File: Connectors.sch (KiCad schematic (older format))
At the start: 0 parts

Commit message: Added symbols to new sheet.
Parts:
- added J?: Conn_01x09, symbol Connector_Generic:Conn_01x09
- added J? (x2): Conn_01x04, symbol Connector_Generic:Conn_01x04
- added J?: Conn_02x03_Odd_Even, symbol Connector_Generic:Conn_02x03_Odd_Even
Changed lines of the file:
@@
 Comment4 "Aurthor: Brycen Dhom"
 $EndDescr
+$Comp
+L Connector_Generic:Conn_01x09 J?
+U 1 1 60175092
+P 3625 3575
+F 0 "J?" H 3705 3617 50  0000 L CNN
+F 1 "Conn_01x09" H 3705 3526 50  0000 L CNN
+F 2 "" H 3625 3575 50  0001 C CNN
+F 3 "~" H 3625 3575 50  0001 C CNN
+	1    3625 3575
+	1    0    0    -1
+$EndComp
+$Comp
+L Connector_Generic:Conn_01x04 J?
+U 1 1 60176115
+P 4775 3300
+F 0 "J?" H 4855 3292 50  0000 L CNN
+F 1 "Conn_01x04" H 4855 3201 50  0000 L CNN
+F 2 "" H 4775 3300 50  0001 C CNN
+F 3 "~" H 4775 3300 50  0001 C CNN
+	1    4775 3300
+	1    0    0    -1
+$EndComp
+$Comp
+L Connector_Generic:Conn_02x03_Odd_Even J?
+U 1 1 6017679C
+P 3575 4650
+F 0 "J?" H 3625 4967 50  0000 C CNN
+F 1 "Conn_02x03_Odd_Even" H 3625 4876 50  0000 C CNN
+F 2 "" H 3575 4650 50  0001 C CNN
+F 3 "~" H 3575 4650 50  0001 C CNN
+	1    3575 4650
+	1    0    0    -1
+$EndComp
+$Comp
+L Connector_Generic:Conn_01x04 J?
+U 1 1 6017766B
+P 4725 4525
+F 0 "J?" H 4805 4517 50  0000 L CNN
+F 1 "Conn_01x04" H 4805 4426 50  0000 L CNN
+F 2 "" H 4725 4525 50  0001 C CNN
+F 3 "~" H 4725 4525 50  0001 C CNN
+	1    4725 4525
+	1    0    0    -1
+$EndComp
 $EndSCHEMATC

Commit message: Added footprint associations.
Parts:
- J1: renamed from J?; value Conn_01x09 -> Digital Pins; footprint (none) -> Connector_PinSocket_2.54mm:PinSocket_1x09_P2.54mm_Vertical
- J2: renamed from J?; value Conn_01x04 -> Serial; footprint (none) -> Connector_PinSocket_2.54mm:PinSocket_1x04_P2.54mm_Vertical
- J3: renamed from J?; value Conn_02x03_Odd_Even -> ICSP; footprint (none) -> Connector_PinSocket_2.54mm:PinSocket_2x03_P2.54mm_Vertical
- J4: renamed from J?; value Conn_01x04 -> I2C; footprint (none) -> Connector_PinSocket_2.54mm:PinSocket_1x04_P2.54mm_Vertical
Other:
- moved on the sheet: J1, J2, J3, J4
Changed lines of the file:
@@
 $EndDescr
 $Comp
-L Connector_Generic:Conn_01x09 J?
+L Connector_Generic:Conn_01x09 J1
 U 1 1 60175092
-P 3625 3575
-F 0 "J?" H 3705 3617 50  0000 L CNN
-F 1 "Conn_01x09" H 3705 3526 50  0000 L CNN
-F 2 "" H 3625 3575 50  0001 C CNN
-F 3 "~" H 3625 3575 50  0001 C CNN
-	1    3625 3575
+P 3650 3525
+F 0 "J1" H 3730 3567 50  0000 L CNN
+F 1 "Digital Pins" H 3730 3476 50  0000 L CNN
+F 2 "Connector_PinSocket_2.54mm:PinSocket_1x09_P2.54mm_Vertical" H 3650 3525 50  0001 C CNN
+F 3 "~" H 3650 3525 50  0001 C CNN
+	1    3650 3525
 	1    0    0    -1
 $EndComp
 $Comp
-L Connector_Generic:Conn_01x04 J?
+L Connector_Generic:Conn_01x04 J2
 U 1 1 60176115
-P 4775 3300
-F 0 "J?" H 4855 3292 50  0000 L CNN
-F 1 "Conn_01x04" H 4855 3201 50  0000 L CNN
-F 2 "" H 4775 3300 50  0001 C CNN
-F 3 "~" H 4775 3300 50  0001 C CNN
-	1    4775 3300
+P 3900 1350
+F 0 "J2" H 3980 1342 50  0000 L CNN
+F 1 "Serial" H 3980 1251 50  0000 L CNN
+F 2 "Connector_PinSocket_2.54mm:PinSocket_1x04_P2.54mm_Vertical" H 3900 1350 50  0001 C CNN
+F 3 "~" H 3900 1350 50  0001 C CNN
+	1    3900 1350
 	1    0    0    -1
 $EndComp
 $Comp
-L Connector_Generic:Conn_02x03_Odd_Even J?
+L Connector_Generic:Conn_02x03_Odd_Even J3
 U 1 1 6017679C
-P 3575 4650
-F 0 "J?" H 3625 4967 50  0000 C CNN
-F 1 "Conn_02x03_Odd_Even" H 3625 4876 50  0000 C CNN
-F 2 "" H 3575 4650 50  0001 C CNN
-F 3 "~" H 3575 4650 50  0001 C CNN
-	1    3575 4650
+P 4975 3575
+F 0 "J3" H 5025 3892 50  0000 C CNN
+F 1 "ICSP" H 5025 3801 50  0000 C CNN
+F 2 "Connector_PinSocket_2.54mm:PinSocket_2x03_P2.54mm_Vertical" H 4975 3575 50  0001 C CNN
+F 3 "~" H 4975 3575 50  0001 C CNN
+	1    4975 3575
 	1    0    0    -1
 $EndComp
 $Comp
-L Connector_Generic:Conn_01x04 J?
+L Connector_Generic:Conn_01x04 J4
 U 1 1 6017766B
-P 4725 4525
-F 0 "J?" H 4805 4517 50  0000 L CNN
-F 1 "Conn_01x04" H 4805 4426 50  0000 L CNN
-F 2 "" H 4725 4525 50  0001 C CNN
-F 3 "~" H 4725 4525 50  0001 C CNN
-	1    4725 4525
+P 5125 1275
+F 0 "J4" H 5205 1267 50  0000 L CNN
+F 1 "I2C" H 5205 1176 50  0000 L CNN
+F 2 "Connector_PinSocket_2.54mm:PinSocket_1x04_P2.54mm_Vertical" H 5125 1275 50  0001 C CNN
+F 3 "~" H 5125 1275 50  0001 C CNN
+	1    5125 1275
 	1    0    0    -1
 $EndComp

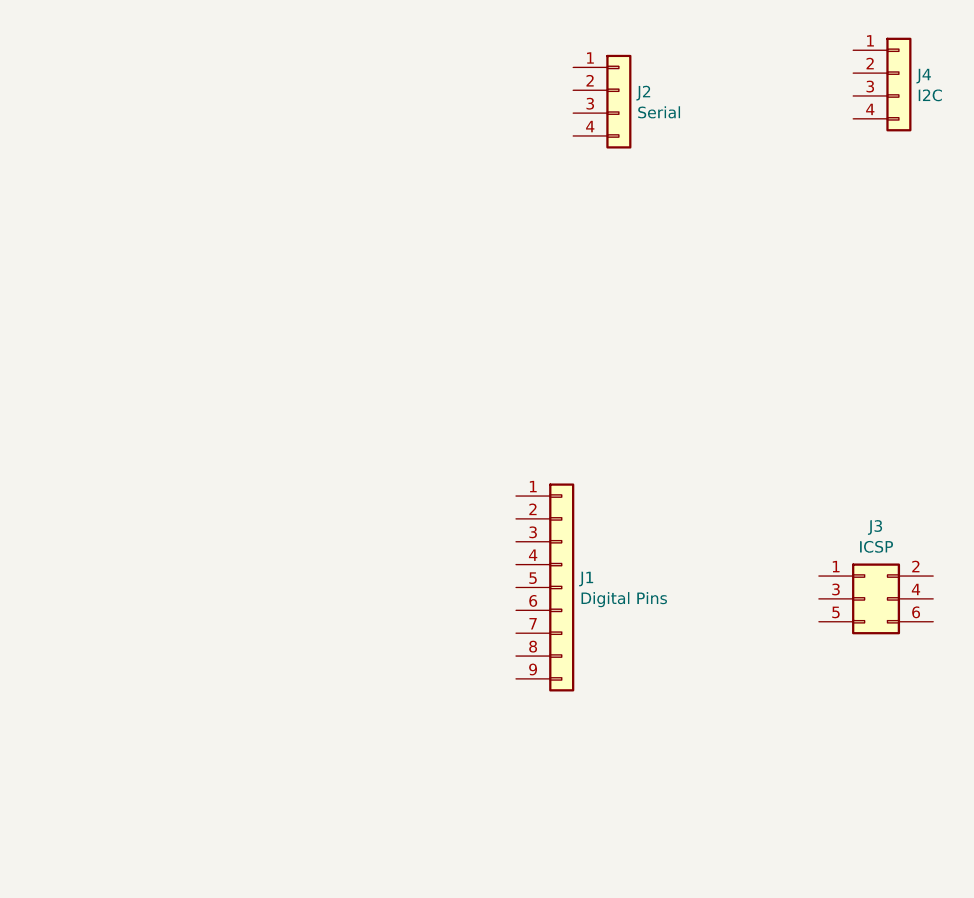
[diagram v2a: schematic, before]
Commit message: Added wiring in connectors sheet.
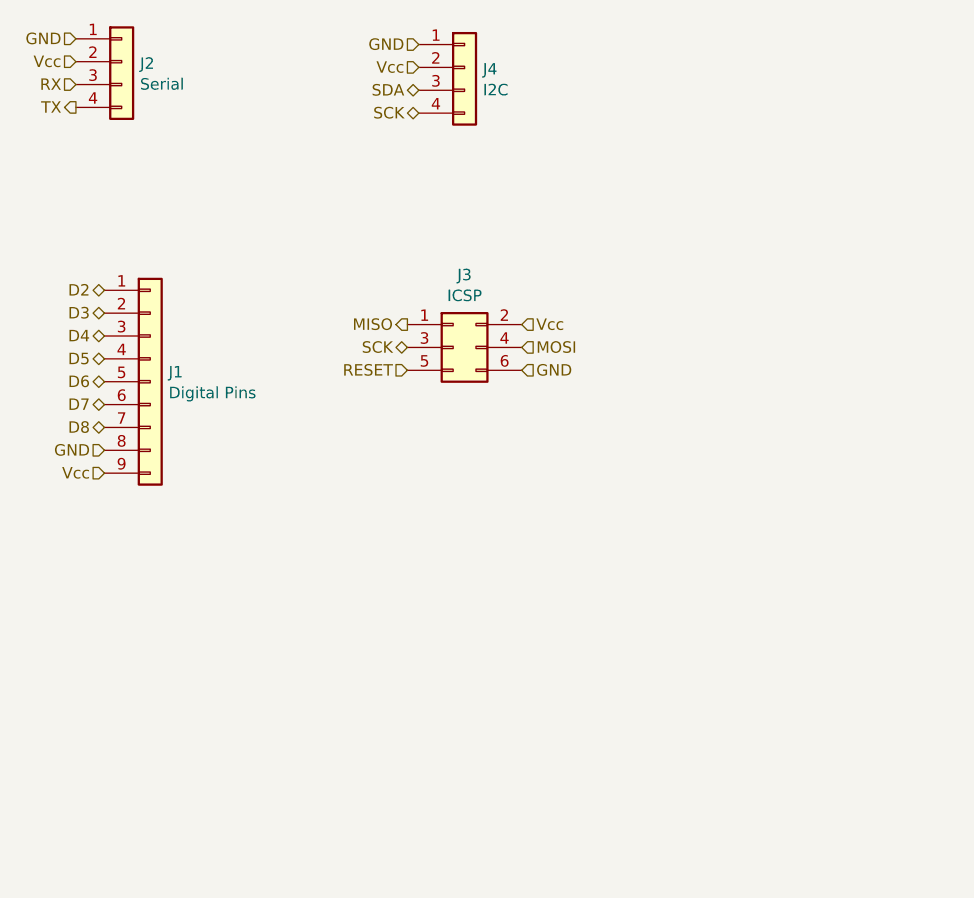
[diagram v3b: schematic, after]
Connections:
- net D2: now reaches J1.1 (Pin_1)
- net D3: now reaches J1.2 (Pin_2)
- net D4: now reaches J1.3 (Pin_3)
- net D5: now reaches J1.4 (Pin_4)
- net D6: now reaches J1.5 (Pin_5)
- net D7: now reaches J1.6 (Pin_6)
- net D8: now reaches J1.7 (Pin_7)
- net GND: now reaches J1.8 (Pin_8)
- net GND: now also J2.1 (Pin_1), J3.6 (Pin_6), J4.1 (Pin_1)
- net Vcc: now reaches J1.9 (Pin_9)
- net Vcc: now also J2.2 (Pin_2), J3.2 (Pin_2), J4.2 (Pin_2)
- net RX: now reaches J2.3 (Pin_3)
- net TX: now reaches J2.4 (Pin_4)
- net MISO: now reaches J3.1 (Pin_1)
- net SCK: now reaches J3.3 (Pin_3)
- net SCK: now also J4.4 (Pin_4)
- net MOSI: now reaches J3.4 (Pin_4)
- net RESET: now reaches J3.5 (Pin_5)
- net SDA: now reaches J4.3 (Pin_3)
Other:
- moved on the sheet: J1, J2, J3, J4
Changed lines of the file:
@@
 L Connector_Generic:Conn_01x09 J1
 U 1 1 60175092
-P 3650 3525
-F 0 "J1" H 3730 3567 50  0000 L CNN
-F 1 "Digital Pins" H 3730 3476 50  0000 L CNN
-F 2 "Connector_PinSocket_2.54mm:PinSocket_1x09_P2.54mm_Vertical" H 3650 3525 50  0001 C CNN
-F 3 "~" H 3650 3525 50  0001 C CNN
-	1    3650 3525
+P 1850 2625
+F 0 "J1" H 1930 2667 50  0000 L CNN
+F 1 "Digital Pins" H 1930 2576 50  0000 L CNN
+F 2 "Connector_PinSocket_2.54mm:PinSocket_1x09_P2.54mm_Vertical" H 1850 2625 50  0001 C CNN
+F 3 "~" H 1850 2625 50  0001 C CNN
+	1    1850 2625
 	1    0    0    -1
 $EndComp
@@
 L Connector_Generic:Conn_01x04 J2
 U 1 1 60176115
-P 3900 1350
-F 0 "J2" H 3980 1342 50  0000 L CNN
-F 1 "Serial" H 3980 1251 50  0000 L CNN
-F 2 "Connector_PinSocket_2.54mm:PinSocket_1x04_P2.54mm_Vertical" H 3900 1350 50  0001 C CNN
-F 3 "~" H 3900 1350 50  0001 C CNN
-	1    3900 1350
+P 1725 1225
+F 0 "J2" H 1805 1217 50  0000 L CNN
+F 1 "Serial" H 1805 1126 50  0000 L CNN
+F 2 "Connector_PinSocket_2.54mm:PinSocket_1x04_P2.54mm_Vertical" H 1725 1225 50  0001 C CNN
+F 3 "~" H 1725 1225 50  0001 C CNN
+	1    1725 1225
 	1    0    0    -1
 $EndComp
@@
 L Connector_Generic:Conn_02x03_Odd_Even J3
 U 1 1 6017679C
-P 4975 3575
-F 0 "J3" H 5025 3892 50  0000 C CNN
-F 1 "ICSP" H 5025 3801 50  0000 C CNN
-F 2 "Connector_PinSocket_2.54mm:PinSocket_2x03_P2.54mm_Vertical" H 4975 3575 50  0001 C CNN
-F 3 "~" H 4975 3575 50  0001 C CNN
-	1    4975 3575
+P 3175 2475
+F 0 "J3" H 3225 2792 50  0000 C CNN
+F 1 "ICSP" H 3225 2701 50  0000 C CNN
+F 2 "Connector_PinSocket_2.54mm:PinSocket_2x03_P2.54mm_Vertical" H 3175 2475 50  0001 C CNN
+F 3 "~" H 3175 2475 50  0001 C CNN
+	1    3175 2475
 	1    0    0    -1
 $EndComp
@@
 L Connector_Generic:Conn_01x04 J4
 U 1 1 6017766B
-P 5125 1275
-F 0 "J4" H 5205 1267 50  0000 L CNN
-F 1 "I2C" H 5205 1176 50  0000 L CNN
-F 2 "Connector_PinSocket_2.54mm:PinSocket_1x04_P2.54mm_Vertical" H 5125 1275 50  0001 C CNN
-F 3 "~" H 5125 1275 50  0001 C CNN
-	1    5125 1275
+P 3225 1250
+F 0 "J4" H 3305 1242 50  0000 L CNN
+F 1 "I2C" H 3305 1151 50  0000 L CNN
+F 2 "Connector_PinSocket_2.54mm:PinSocket_1x04_P2.54mm_Vertical" H 3225 1250 50  0001 C CNN
+F 3 "~" H 3225 1250 50  0001 C CNN
+	1    3225 1250
 	1    0    0    -1
 $EndComp
+Text HLabel 2975 2375 0    50   Output ~ 0
+MISO
+Text HLabel 2975 2475 0    50   BiDi ~ 0
+SCK
+Text HLabel 2975 2575 0    50   Input ~ 0
+RESET
+Text HLabel 3475 2375 2    50   Input ~ 0
+Vcc
+Text HLabel 3475 2475 2    50   Input ~ 0
+MOSI
+Text HLabel 3475 2575 2    50   Input ~ 0
+GND
+Text HLabel 1525 1125 0    50   Input ~ 0
+GND
+Text HLabel 1525 1225 0    50   Input ~ 0
+Vcc
+Text HLabel 1525 1325 0    50   Input ~ 0
+RX
+Text HLabel 1525 1425 0    50   Output ~ 0
+TX
+Text HLabel 3025 1150 0    50   Input ~ 0
+GND
+Text HLabel 3025 1250 0    50   Input ~ 0
+Vcc
+Text HLabel 3025 1350 0    50   BiDi ~ 0
+SDA
+Text HLabel 3025 1450 0    50   BiDi ~ 0
+SCK
+Text HLabel 1650 2225 0    50   BiDi ~ 0
+D2
+Text HLabel 1650 2325 0    50   BiDi ~ 0
+D3
+Text HLabel 1650 2525 0    50   BiDi ~ 0
+D5
+Text HLabel 1650 2625 0    50   BiDi ~ 0
+D6
+Text HLabel 1650 2825 0    50   BiDi ~ 0
+D8
+Text HLabel 1650 2425 0    50   BiDi ~ 0
+D4
+Text HLabel 1650 2725 0    50   BiDi ~ 0
+D7
+Text HLabel 1650 2925 0    50   Input ~ 0
+GND
+Text HLabel 1650 3025 0    50   Input ~ 0
+Vcc
 $EndSCHEMATC

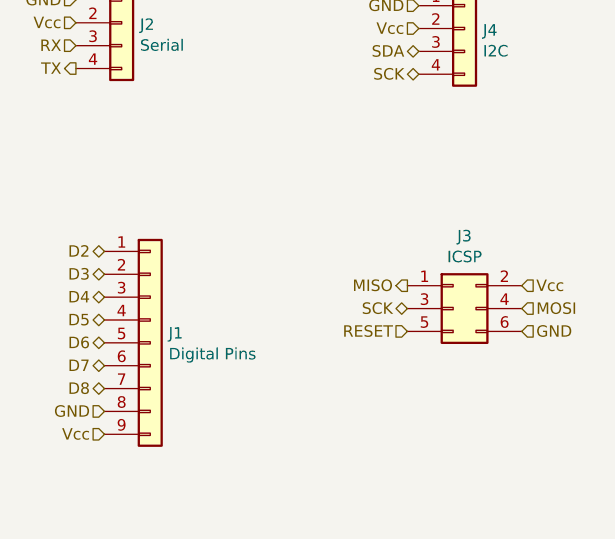
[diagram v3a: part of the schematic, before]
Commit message: Added more necessary components. Corrected winrings. Generated netlist.
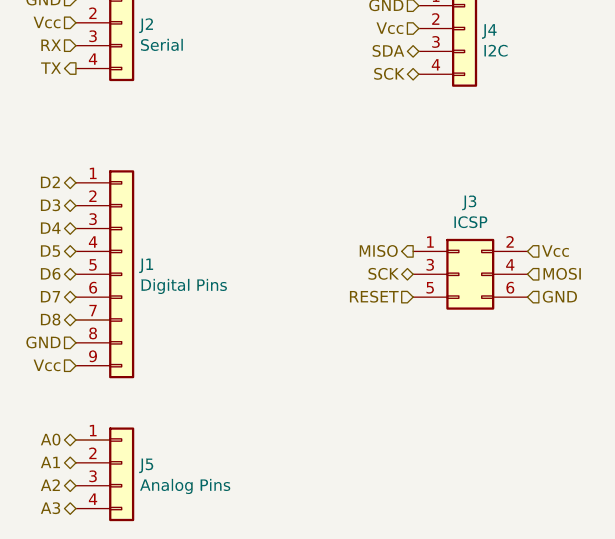
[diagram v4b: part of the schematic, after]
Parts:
- added J5: Analog Pins, Connector_PinSocket_2.54mm:PinSocket_1x04_P2.54mm_Vertical, symbol Connector_Generic:Conn_01x04
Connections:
- new net A0: J5.1 (Pin_1)
- new net A1: J5.2 (Pin_2)
- new net A2: J5.3 (Pin_3)
- new net A3: J5.4 (Pin_4)
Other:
- moved on the sheet: J1, J3
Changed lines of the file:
@@
 L Connector_Generic:Conn_01x09 J1
 U 1 1 60175092
-P 1850 2625
-F 0 "J1" H 1930 2667 50  0000 L CNN
-F 1 "Digital Pins" H 1930 2576 50  0000 L CNN
-F 2 "Connector_PinSocket_2.54mm:PinSocket_1x09_P2.54mm_Vertical" H 1850 2625 50  0001 C CNN
-F 3 "~" H 1850 2625 50  0001 C CNN
-	1    1850 2625
+P 1725 2325
+F 0 "J1" H 1805 2367 50  0000 L CNN
+F 1 "Digital Pins" H 1805 2276 50  0000 L CNN
+F 2 "Connector_PinSocket_2.54mm:PinSocket_1x09_P2.54mm_Vertical" H 1725 2325 50  0001 C CNN
+F 3 "~" H 1725 2325 50  0001 C CNN
+	1    1725 2325
 	1    0    0    -1
 $EndComp
@@
 L Connector_Generic:Conn_02x03_Odd_Even J3
 U 1 1 6017679C
-P 3175 2475
-F 0 "J3" H 3225 2792 50  0000 C CNN
-F 1 "ICSP" H 3225 2701 50  0000 C CNN
-F 2 "Connector_PinSocket_2.54mm:PinSocket_2x03_P2.54mm_Vertical" H 3175 2475 50  0001 C CNN
-F 3 "~" H 3175 2475 50  0001 C CNN
-	1    3175 2475
+P 3200 2325
+F 0 "J3" H 3250 2642 50  0000 C CNN
+F 1 "ICSP" H 3250 2551 50  0000 C CNN
+F 2 "Connector_PinSocket_2.54mm:PinSocket_2x03_P2.54mm_Vertical" H 3200 2325 50  0001 C CNN
+F 3 "~" H 3200 2325 50  0001 C CNN
+	1    3200 2325
 	1    0    0    -1
 $EndComp
@@
 	1    0    0    -1
 $EndComp
-Text HLabel 2975 2375 0    50   Output ~ 0
+Text HLabel 3000 2225 0    50   Output ~ 0
 MISO
-Text HLabel 2975 2475 0    50   BiDi ~ 0
+Text HLabel 3000 2325 0    50   BiDi ~ 0
 SCK
-Text HLabel 2975 2575 0    50   Input ~ 0
+Text HLabel 3000 2425 0    50   Input ~ 0
 RESET
-Text HLabel 3475 2375 2    50   Input ~ 0
+Text HLabel 3500 2225 2    50   Input ~ 0
 Vcc
-Text HLabel 3475 2475 2    50   Input ~ 0
+Text HLabel 3500 2325 2    50   Input ~ 0
 MOSI
-Text HLabel 3475 2575 2    50   Input ~ 0
+Text HLabel 3500 2425 2    50   Input ~ 0
 GND
 Text HLabel 1525 1125 0    50   Input ~ 0
@@
 Text HLabel 3025 1450 0    50   BiDi ~ 0
 SCK
-Text HLabel 1650 2225 0    50   BiDi ~ 0
+Text HLabel 1525 1925 0    50   BiDi ~ 0
 D2
-Text HLabel 1650 2325 0    50   BiDi ~ 0
+Text HLabel 1525 2025 0    50   BiDi ~ 0
 D3
-Text HLabel 1650 2525 0    50   BiDi ~ 0
+Text HLabel 1525 2225 0    50   BiDi ~ 0
 D5
-Text HLabel 1650 2625 0    50   BiDi ~ 0
+Text HLabel 1525 2325 0    50   BiDi ~ 0
 D6
-Text HLabel 1650 2825 0    50   BiDi ~ 0
+Text HLabel 1525 2525 0    50   BiDi ~ 0
 D8
-Text HLabel 1650 2425 0    50   BiDi ~ 0
+Text HLabel 1525 2125 0    50   BiDi ~ 0
 D4
-Text HLabel 1650 2725 0    50   BiDi ~ 0
+Text HLabel 1525 2425 0    50   BiDi ~ 0
 D7
-Text HLabel 1650 2925 0    50   Input ~ 0
+Text HLabel 1525 2625 0    50   Input ~ 0
 GND
-Text HLabel 1650 3025 0    50   Input ~ 0
+Text HLabel 1525 2725 0    50   Input ~ 0
 Vcc
+$Comp
+L Connector_Generic:Conn_01x04 J5
+U 1 1 601D7FB0
+P 1725 3150
+F 0 "J5" H 1805 3142 50  0000 L CNN
+F 1 "Analog Pins" H 1805 3051 50  0000 L CNN
+F 2 "Connector_PinSocket_2.54mm:PinSocket_1x04_P2.54mm_Vertical" H 1725 3150 50  0001 C CNN
+F 3 "~" H 1725 3150 50  0001 C CNN
+	1    1725 3150
+	1    0    0    -1
+$EndComp
+Text HLabel 1525 3050 0    50   BiDi ~ 0
+A0
+Text HLabel 1525 3150 0    50   BiDi ~ 0
+A1
+Text HLabel 1525 3250 0    50   BiDi ~ 0
+A2
+Text HLabel 1525 3350 0    50   BiDi ~ 0
+A3
 $EndSCHEMATC

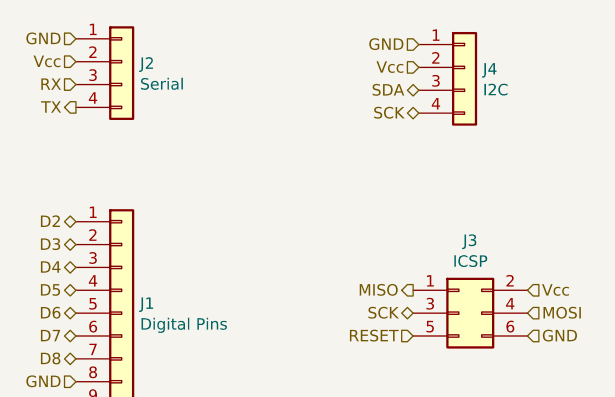
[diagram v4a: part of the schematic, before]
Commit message: Finished PCB Layout.
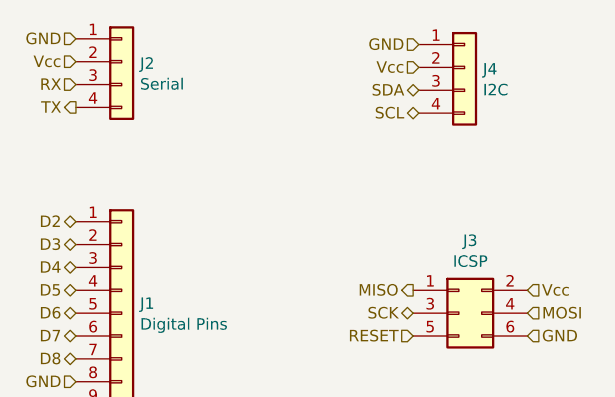
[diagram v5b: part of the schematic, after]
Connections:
- net SCK: no longer J4.4 (Pin_4)
- new net SCL: J4.4 (Pin_4)
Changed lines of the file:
@@
 SDA
 Text HLabel 3025 1450 0    50   BiDi ~ 0
-SCK
+SCL
 Text HLabel 1525 1925 0    50   BiDi ~ 0
 D2
